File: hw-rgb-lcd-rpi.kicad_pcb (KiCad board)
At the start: 2 copper layers, 14 parts, among them J1 lq043t1dg03, J2 minilaptop-lcd, P1 GPIO, P2 I2C, P3 BATT, P4 MINILAP SPARE, P5 P_LED, P6 BACKLIGHT, U1 RPi_A+_B+_2B_Hat

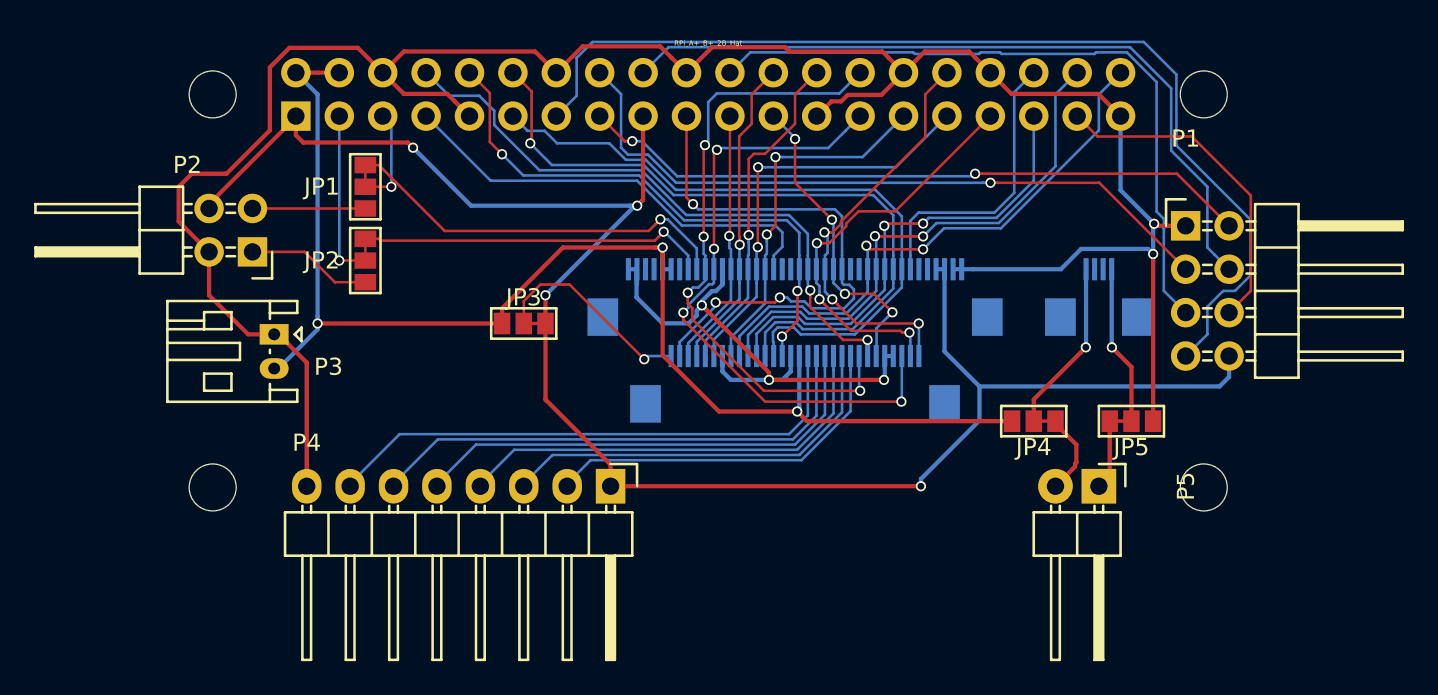
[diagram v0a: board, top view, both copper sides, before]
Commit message: Add GND fill
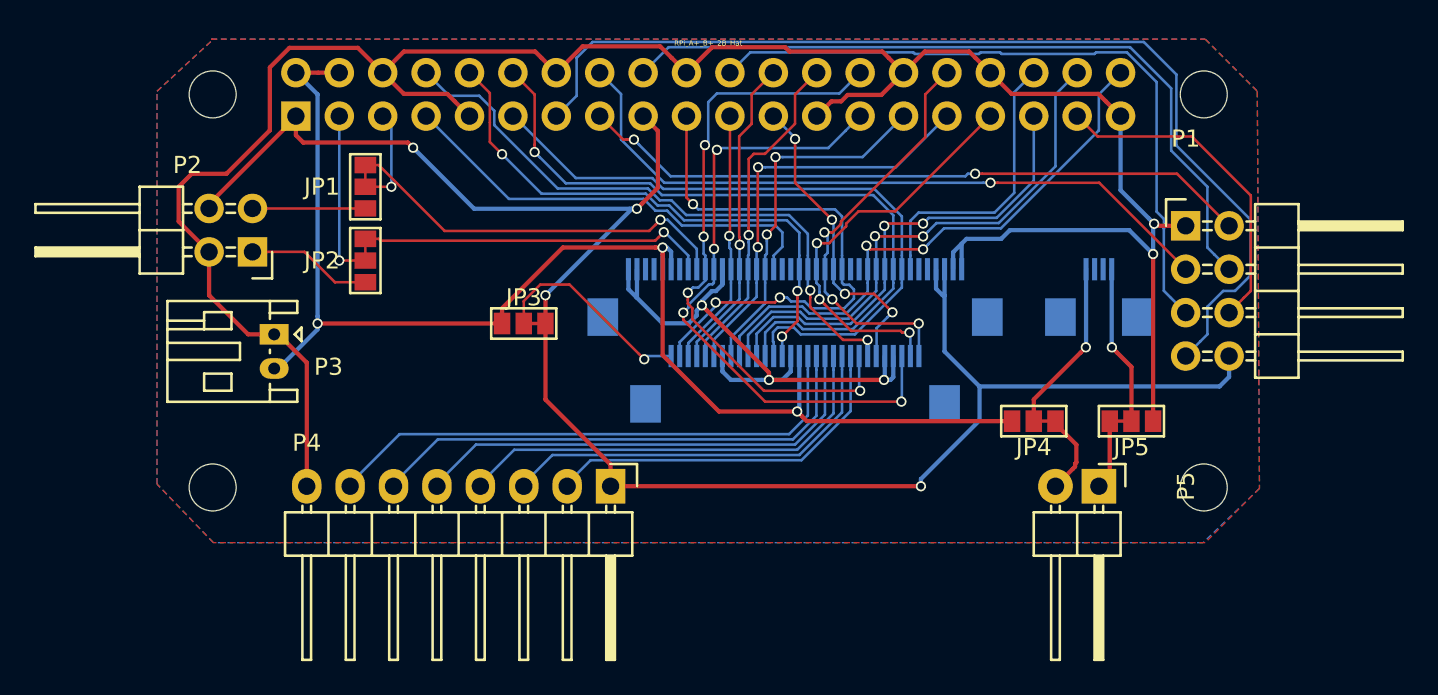
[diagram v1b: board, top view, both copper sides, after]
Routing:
- net GND: track 166.4 -> 171.2 mm
- net VCC: track 104.8 -> 106.9 mm
- net +BATT: track 77.5 -> 78.7 mm
- added copper zone on B.Cu, net GND
- added copper zone on F.Cu, net GND

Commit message: Ensure keepout areas and edge cuts are marked
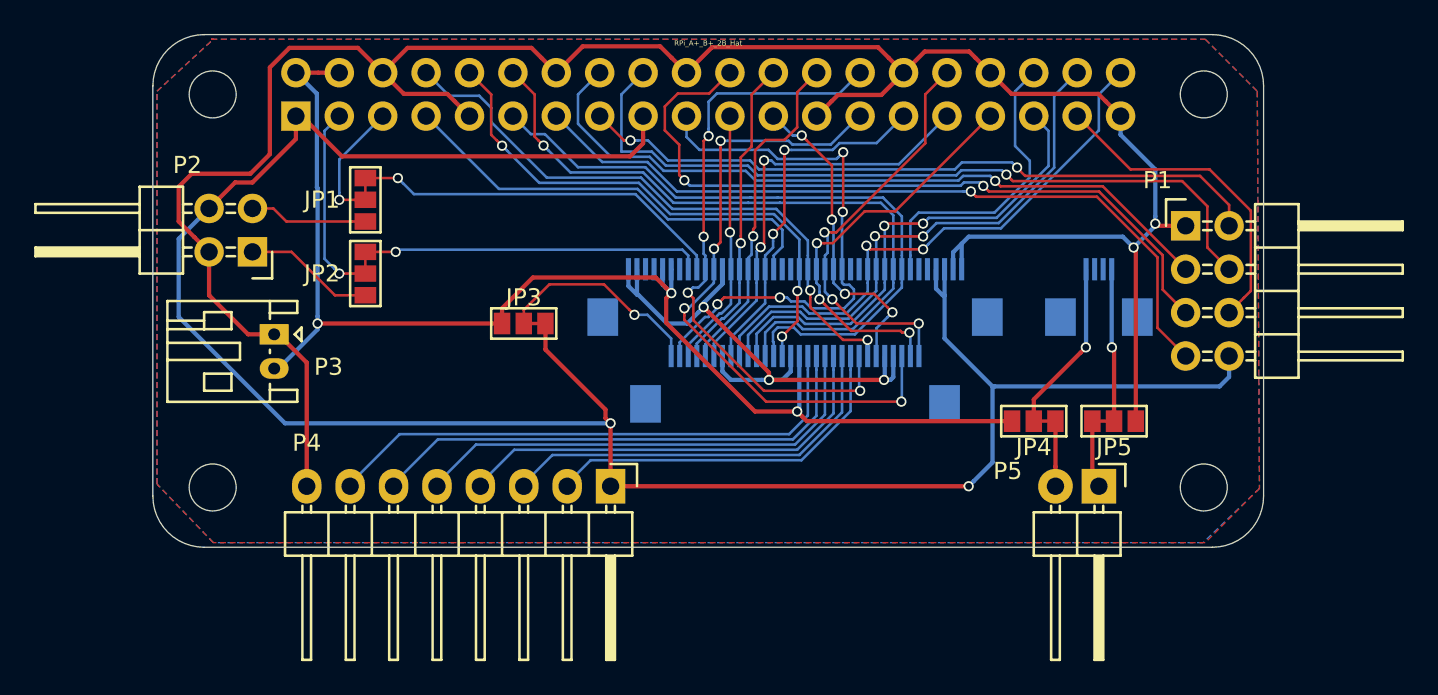
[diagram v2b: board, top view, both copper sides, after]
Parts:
- moved JP5 1.02 mm to (172.3, 113.0)
- moved JP1 0.76 mm to (128.5, 100.1)
- moved JP2 0.76 mm to (128.5, 104.4)
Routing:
- net VCC: track 106.9 -> 129.6 mm, vias 4 -> 2
- net /GPIO27: track 60.4 -> 45.1 mm, vias 0 -> 1
- net +BATT: track 78.7 -> 75.6 mm
- net /GPIO25: track 40.5 -> 43.3 mm, vias 0 -> 2
- net /GPIO23: track 40.6 -> 42.8 mm
- net Net-(JP4-Pad1): track 16.3 -> 15.2 mm
- net /GPIO22: track 39.6 -> 40.6 mm
- net /V_SYNC: track 31.8 -> 32.6 mm
- net /R5: track 27.6 -> 28.3 mm
- net /R2: track 17.1 -> 17.8 mm
- net GND: track 171.2 -> 170.5 mm
- net /GPIO24: track 44.5 -> 45.2 mm, vias 0 -> 1
- net /G2: track 32.3 -> 32.9 mm, vias 3 -> 4
- net /R4: track 42.3 -> 41.7 mm
- net Net-(JP5-Pad2): track 14.7 -> 14.2 mm
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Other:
- board outline added: 65 x 30 mm

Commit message: Add labels and adjust silkscreen for all parts
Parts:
- added REF***: OSHW-Logo_5.7x6mm_SilkScreen, Symbols:OSHW-Logo_5.7x6mm_SilkScreen, F.Cu at (158.6, 116.6)
- JP1: value J_HSYNC -> HSYNC
- JP2: value J_VSYNC -> VSYNC
- JP3: value 3v3_5v -> 5v 3v3
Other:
- board text added: "- +"
- board text added: "I2C"
- board text added: "http://github.com/hamishcoleman/ hw-rgb-lcd-rpi"
